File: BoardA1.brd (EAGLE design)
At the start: 43.2 x 100 mm, 17 parts, among them J1 LOAD_CELL1X03-PTH, J2 CONN_12X2, J3 LOAD_CELL1X03-PTH, J5 LOAD_CELL1X03-PTH, J6 LOAD_CELL1X03-PTH

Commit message: Starting Routing Board
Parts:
- moved C3 25.4 mm to (11.4, 59.7), turned to 180 degrees
- moved R3 23.4 mm to (31.8, 90.2), turned to 180 degrees
- moved C2 21.6 mm to (5.08, 58.4)
- moved R1 20.1 mm to (27.9, 86.4), turned to 180 degrees
- moved C4 15.2 mm to (29.2, 58.4)
- moved U$2 14.0 mm to (33.0, 71.1), turned to 270 degrees
- moved R6 7.41 mm to (8.89, 92.7), turned to 180 degrees
- moved R5 5.24 mm to (10.2, 85.1), turned to 0 degrees
- moved U$3 1.80 mm to (10.2, 71.1), turned to 270 degrees
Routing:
- net GND: track 0.00 -> 106.2 mm
- net +15V: track 0.00 -> 46.5 mm
- net -15V: track 0.00 -> 41.1 mm
- net -SIG1: track 0.00 -> 32.5 mm
- net -EX2: track 0.00 -> 29.5 mm
- net +EX2: track 0.00 -> 28.7 mm
- net -SIG2: track 0.00 -> 28.0 mm
- net -EX1: track 0.00 -> 23.6 mm
- net +EX1: track 0.00 -> 22.9 mm
- net 5V: track 0.00 -> 19.1 mm
- net +SIG2: track 0.00 -> 14.5 mm
- net +SIG1: track 0.00 -> 13.3 mm
- net N$3: track 0.00 -> 12.8 mm
- net N$1: track 0.00 -> 10.3 mm
- net N$2: track 0.00 -> 7.10 mm

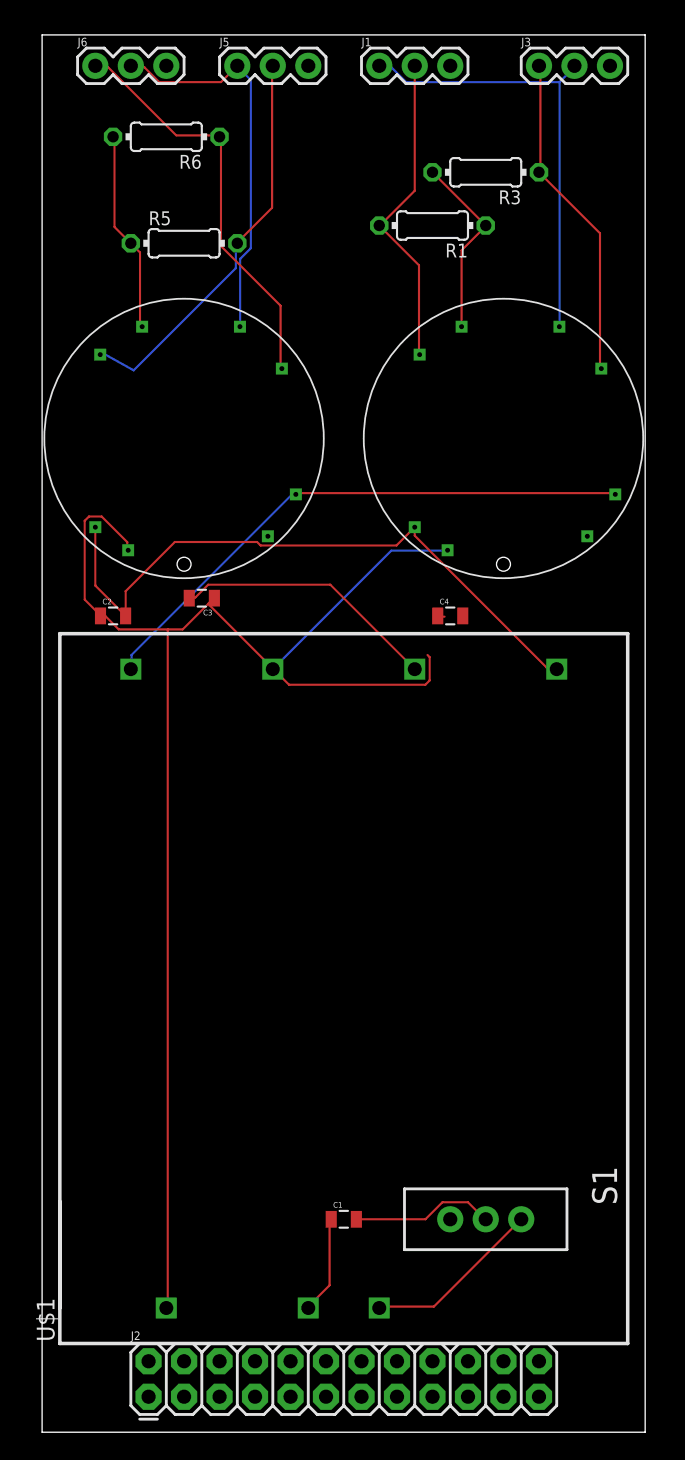
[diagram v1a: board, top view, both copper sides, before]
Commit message: routed Top Layer Board
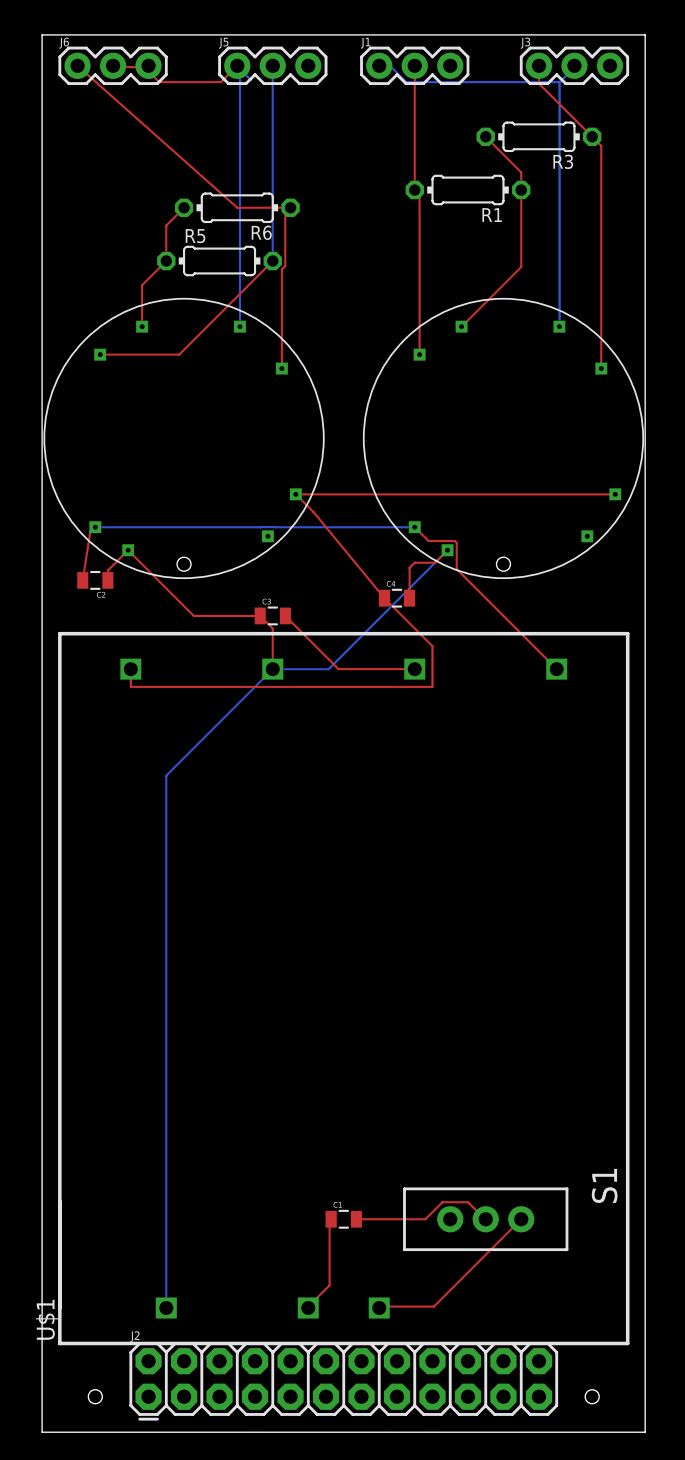
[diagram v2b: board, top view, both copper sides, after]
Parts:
- moved R6 7.18 mm to (14.0, 87.6)
- moved C3 5.24 mm to (16.5, 58.4), turned to 0 degrees
- moved R3 4.58 mm to (35.6, 92.7)
- moved C4 4.02 mm to (25.4, 59.7)
- moved R1 3.59 mm to (30.5, 88.9)
- moved R5 2.84 mm to (12.7, 83.8)
- moved C2 2.84 mm to (3.81, 61.0), turned to 180 degrees
- moved J6 1.27 mm to (2.54, 97.8)
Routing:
- net -15V: track 41.1 -> 63.3 mm
- net GND: track 106.2 -> 88.7 mm
- net 5V: track 19.1 -> 10.8 mm
- net +SIG2: track 14.5 -> 9.95 mm
- net +15V: track 46.5 -> 42.3 mm
- net +SIG1: track 13.3 -> 16.5 mm
- net -SIG2: track 28.0 -> 30.1 mm
- net +EX1: track 22.9 -> 21.0 mm
- net -EX2: track 29.5 -> 31.0 mm

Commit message: updated
added holes to attach boards
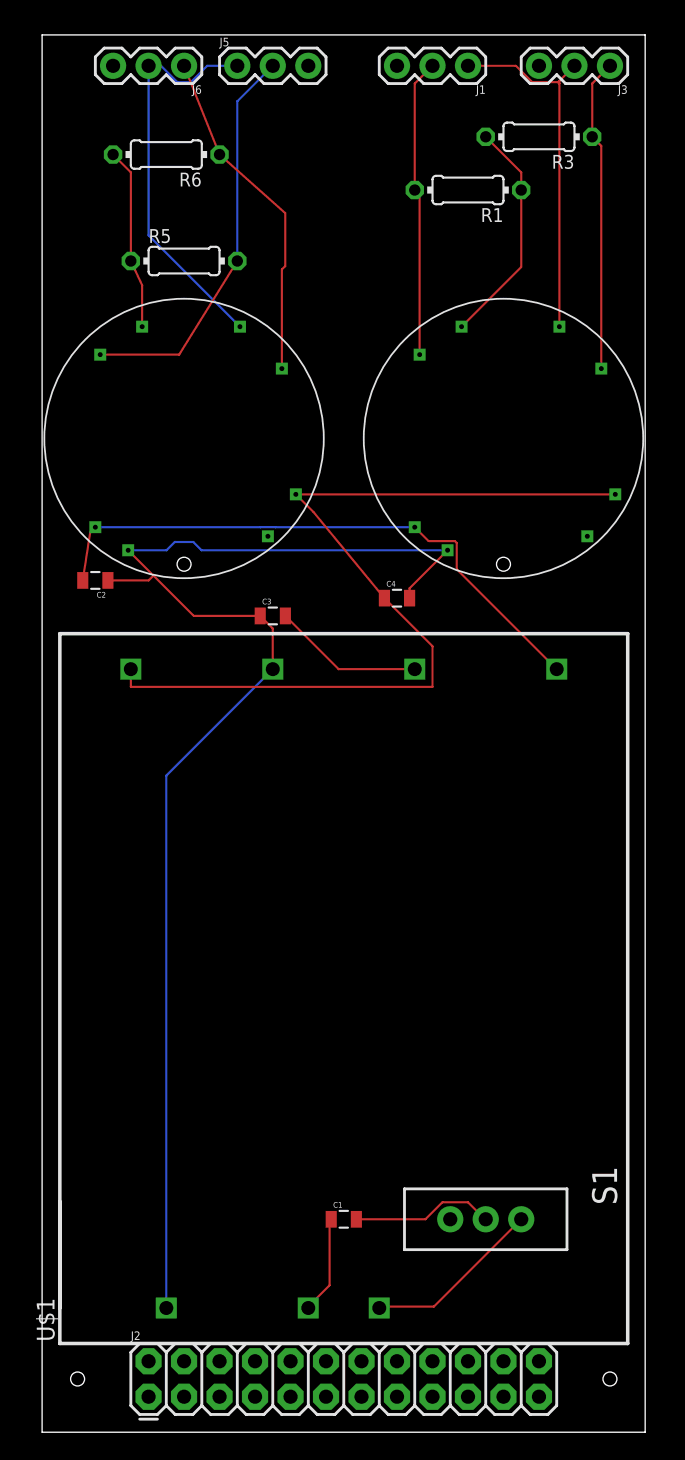
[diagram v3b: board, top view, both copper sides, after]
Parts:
- moved J6 7.62 mm to (10.2, 97.8), turned to 180 degrees
- moved J1 6.35 mm to (30.5, 97.8), turned to 180 degrees
- moved R6 6.35 mm to (8.89, 91.4)
- moved J3 5.08 mm to (40.6, 97.8), turned to 180 degrees
- moved R5 2.54 mm to (10.2, 83.8)
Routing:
- net GND: track 88.7 -> 95.8 mm
- net -EX2: track 31.0 -> 24.5 mm
- net -SIG1: track 32.5 -> 26.2 mm
- net +SIG2: track 9.95 -> 13.2 mm
- net -EX1: track 23.8 -> 22.6 mm
- net -SIG2: track 30.1 -> 29.1 mm
- net +EX2: track 29.2 -> 28.7 mm
- net +EX1: track 21.0 -> 21.5 mm

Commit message: update 2.0
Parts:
- moved J6 5.68 mm to (15.2, 95.2)
- moved R6 5.08 mm to (14.0, 91.4)
- moved J5 3.81 mm to (10.2, 97.8)
- moved R5 2.54 mm to (10.2, 86.4)
- moved J1 1.27 mm to (29.2, 97.8)
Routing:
- net -SIG2: track 29.1 -> 21.3 mm
- net -EX2: track 24.5 -> 20.4 mm
- net -SIG1: track 26.2 -> 27.5 mm
- net +SIG2: track 13.2 -> 14.2 mm
- net +EX2: track 28.7 -> 27.7 mm
- net +EX1: track 21.5 -> 21.0 mm
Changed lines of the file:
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@@
 <element name="C3" library="SparkFun-Capacitors" package="0805" value="" x="16.51" y="58.42"/>
 <element name="C4" library="SparkFun-Capacitors" package="0805" value="" x="25.4" y="59.69"/>
-<element name="J1" library="Smartcrutches" package="1X03" value="LOAD_CELL1X03-PTH" x="30.48" y="97.79" rot="R180">
-<attribute name="SF_ID" value="SEN-10245" x="30.48" y="97.79" size="1.778" layer="27" rot="R180" display="off"/>
+<element name="J1" library="Smartcrutches" package="1X03" value="LOAD_CELL1X03-PTH" x="29.21" y="97.79" rot="R180">
+<attribute name="SF_ID" value="SEN-10245" x="29.21" y="97.79" size="1.778" layer="27" rot="R180" display="off"/>
 </element>
 <element name="J3" library="Smartcrutches" package="1X03" value="LOAD_CELL1X03-PTH" x="40.64" y="97.79" rot="R180">
 <attribute name="SF_ID" value="SEN-10245" x="40.64" y="97.79" size="1.778" layer="27" rot="R180" display="off"/>
 </element>
-<element name="J5" library="Smartcrutches" package="1X03" value="LOAD_CELL1X03-PTH" x="13.97" y="97.79">
-<attribute name="SF_ID" value="SEN-10245" x="13.97" y="97.79" size="1.778" layer="27" display="off"/>
-</element>
-<element name="J6" library="Smartcrutches" package="1X03" value="LOAD_CELL1X03-PTH" x="10.16" y="97.79" rot="R180">
-<attribute name="SF_ID" value="SEN-10245" x="10.16" y="97.79" size="1.778" layer="27" rot="R180" display="off"/>
+<element name="J5" library="Smartcrutches" package="1X03" value="LOAD_CELL1X03-PTH" x="10.16" y="97.79">
+<attribute name="SF_ID" value="SEN-10245" x="10.16" y="97.79" size="1.778" layer="27" display="off"/>
+</element>
+<element name="J6" library="Smartcrutches" package="1X03" value="LOAD_CELL1X03-PTH" x="15.24" y="95.25" rot="R180">
+<attribute name="SF_ID" value="SEN-10245" x="15.24" y="95.25" size="1.778" layer="27" rot="R180" display="off"/>
 </element>
 <element name="R1" library="eagle-ltspice" library_urn="urn:adsk.eagle:library:217" package="0204/7" value="" x="30.48" y="88.9" rot="R180">
@@
 <attribute name="SPICEPREFIX" value="R" x="35.56" y="92.71" size="1.778" layer="27" rot="R180" display="off"/>
 </element>
-<element name="R5" library="eagle-ltspice" library_urn="urn:adsk.eagle:library:217" package="0204/7" value="" x="10.16" y="83.82">
-<attribute name="SPICEMODEL" value="NONE" x="10.16" y="83.82" size="1.778" layer="27" display="off"/>
-<attribute name="SPICEPREFIX" value="R" x="10.16" y="83.82" size="1.778" layer="27" display="off"/>
-</element>
-<element name="R6" library="eagle-ltspice" library_urn="urn:adsk.eagle:library:217" package="0204/7" value="" x="8.89" y="91.44" rot="R180">
-<attribute name="SPICEMODEL" value="NONE" x="8.89" y="91.44" size="1.778" layer="27" rot="R180" display="off"/>
-<attribute name="SPICEPREFIX" value="R" x="8.89" y="91.44" size="1.778" layer="27" rot="R180" display="off"/>
+<element name="R5" library="eagle-ltspice" library_urn="urn:adsk.eagle:library:217" package="0204/7" value="" x="10.16" y="86.36">
+<attribute name="SPICEMODEL" value="NONE" x="10.16" y="86.36" size="1.778" layer="27" display="off"/>
+<attribute name="SPICEPREFIX" value="R" x="10.16" y="86.36" size="1.778" layer="27" display="off"/>
+</element>
+<element name="R6" library="eagle-ltspice" library_urn="urn:adsk.eagle:library:217" package="0204/7" value="" x="13.97" y="91.44" rot="R180">
+<attribute name="SPICEMODEL" value="NONE" x="13.97" y="91.44" size="1.778" layer="27" rot="R180" display="off"/>
+<attribute name="SPICEPREFIX" value="R" x="13.97" y="91.44" size="1.778" layer="27" rot="R180" display="off"/>
 </element>
 <element name="S1" library="SparkFun-Electromechanical" package="SWITCH-SPDT" value="" x="31.75" y="15.24" rot="R270">
@@
 <wire x1="37.02" y1="96.52" x2="37.02" y2="96.71" width="0.1524" layer="1"/>
 <wire x1="37.02" y1="96.71" x2="38.1" y2="97.79" width="0.1524" layer="1"/>
-<wire x1="30.48" y1="97.79" x2="33.90763125" y2="97.79" width="0.1524" layer="1"/>
+<wire x1="29.21" y1="97.79" x2="33.90763125" y2="97.79" width="0.1524" layer="1"/>
 <wire x1="36.9184" y1="96.6216" x2="37.02" y2="96.52" width="0.1524" layer="1"/>
 <wire x1="33.90763125" y1="97.79" x2="35.07603125" y2="96.6216" width="0.1524" layer="1"/>
@@
 <wire x1="27.02" y1="77.12" x2="27.02" y2="88.55" width="0.1524" layer="1"/>
 <wire x1="27.02" y1="88.55" x2="26.67" y2="88.9" width="0.1524" layer="1"/>
-<wire x1="26.67" y1="88.9" x2="26.67" y2="96.52" width="0.1524" layer="1"/>
-<wire x1="26.67" y1="96.52" x2="27.94" y2="97.79" width="0.1524" layer="1"/>
+<wire x1="26.67" y1="88.9" x2="26.67" y2="97.79" width="0.1524" layer="1"/>
 </signal>
 <signal name="-EX2">
@@
 <wire x1="17.16" y1="76.12" x2="17.16" y2="83.2127625" width="0.1524" layer="1"/>
 <wire x1="17.16" y1="83.2127625" x2="17.399" y2="83.4517625" width="0.1524" layer="1"/>
-<wire x1="12.7" y1="91.44" x2="17.399" y2="87.249" width="0.1524" layer="1"/>
+<wire x1="17.78" y1="91.44" x2="17.399" y2="87.249" width="0.1524" layer="1"/>
 <wire x1="17.399" y1="83.4517625" x2="17.399" y2="87.249" width="0.1524" layer="1"/>
-<wire x1="10.16" y1="97.79" x2="12.7" y2="91.44" width="0.1524" layer="1"/>
+<wire x1="15.24" y1="95.25" x2="15.24" y2="93.98" width="0.1524" layer="1"/>
+<wire x1="15.24" y1="93.98" x2="17.78" y2="91.44" width="0.1524" layer="1"/>
 </signal>
 <signal name="-SIG2">
@@
 <contactref element="J6" pad="2"/>
 <contactref element="J5" pad="1"/>
-<wire x1="14.1732" y1="79.248" x2="14.16" y2="79.12" width="0.1524" layer="16"/>
-<wire x1="13.97" y1="97.79" x2="14.16" y2="97.6" width="0.1524" layer="16"/>
-<wire x1="9.67603125" y1="96.6216" x2="10.64396875" y2="96.6216" width="0.1524" layer="16"/>
-<wire x1="7.62" y1="97.79" x2="8.50763125" y2="97.79" width="0.1524" layer="16"/>
-<wire x1="11.81236875" y1="97.79" x2="13.97" y2="97.79" width="0.1524" layer="16"/>
-<wire x1="8.50763125" y1="97.79" x2="9.67603125" y2="96.6216" width="0.1524" layer="16"/>
-<wire x1="10.64396875" y1="96.6216" x2="11.81236875" y2="97.79" width="0.1524" layer="16"/>
-<wire x1="14.16" y1="79.12" x2="7.62" y2="85.66" width="0.1524" layer="16"/>
-<wire x1="7.62" y1="85.66" x2="7.62" y2="97.79" width="0.1524" layer="16"/>
+<wire x1="14.16" y1="79.12" x2="14.1732" y2="79.248" width="0.1524" layer="16"/>
+<wire x1="9.77763125" y1="96.52" x2="9.67603125" y2="96.6216" width="0.1524" layer="16"/>
+<wire x1="12.7" y1="92.6972375" x2="12.7" y2="95.25" width="0.1524" layer="16"/>
+<wire x1="12.7" y1="92.6972375" x2="11.811" y2="91.8082375" width="0.1524" layer="16"/>
+<wire x1="11.811" y1="91.8082375" x2="11.811" y2="81.469" width="0.1524" layer="16"/>
+<wire x1="11.811" y1="81.469" x2="14.16" y2="79.12" width="0.1524" layer="16"/>
+<wire x1="12.7" y1="95.25" x2="10.16" y2="97.79" width="0.1524" layer="16"/>
+<wire x1="10.16" y1="97.79" x2="9.67603125" y2="96.6216" width="0" layer="19" extent="16-16"/>
 </signal>
 <signal name="+SIG2">
@@
 <wire x1="7.0104" y1="79.248" x2="7.16" y2="79.12" width="0.1524" layer="1"/>
 <wire x1="7.16" y1="79.12" x2="7.16" y2="82.09" width="0.1524" layer="1"/>
-<wire x1="7.16" y1="82.09" x2="6.35" y2="83.82" width="0.1524" layer="1"/>
-<wire x1="6.35" y1="83.82" x2="6.35" y2="90.17" width="0.1524" layer="1"/>
-<wire x1="6.35" y1="90.17" x2="5.08" y2="91.44" width="0.1524" layer="1"/>
+<wire x1="7.16" y1="82.09" x2="6.35" y2="86.36" width="0.1524" layer="1"/>
+<wire x1="6.35" y1="86.36" x2="6.35" y2="87.63" width="0.1524" layer="1"/>
+<wire x1="6.35" y1="87.63" x2="10.16" y2="91.44" width="0.1524" layer="1"/>
 </signal>
 <signal name="+EX2">
@@
 <contactref element="R5" pad="2"/>
 <contactref element="J5" pad="2"/>
-<wire x1="16.51" y1="97.79" x2="16.4592" y2="97.6884" width="0.1524" layer="1"/>
 <wire x1="4.16" y1="77.12" x2="9.81" y2="77.12" width="0.1524" layer="1"/>
-<wire x1="9.81" y1="77.12" x2="13.97" y2="83.82" width="0.1524" layer="1"/>
-<wire x1="13.97" y1="83.82" x2="13.97" y2="95.25" width="0.1524" layer="16"/>
-<wire x1="13.97" y1="95.25" x2="16.51" y2="97.79" width="0.1524" layer="16"/>
+<wire x1="9.81" y1="77.12" x2="13.97" y2="86.36" width="0.1524" layer="1"/>
+<wire x1="13.97" y1="86.36" x2="13.97" y2="96.52" width="0.1524" layer="16"/>
+<wire x1="13.97" y1="96.52" x2="12.7" y2="97.79" width="0.1524" layer="16"/>
 </signal>
 <signal name="N$4">

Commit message: Updated both Boards
- Added holes
- Changed connectors
- routed both Boards
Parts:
- J2: value CONN_12X2 -> FEMALE 2x3; device Smartcrutches:2X12 -> SparkFun-Connectors:2X3
- moved J2 14.4 mm to (22.0, 2.00)
- moved J3 2.54 mm to (38.1, 97.8)
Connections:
- net 5V: now also J2.1
- net GND: now also J2.3
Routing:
- net 5V: track 10.8 -> 65.5 mm
- net GND: track 95.8 -> 114.3 mm
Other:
- board size 43.2 x 100 mm -> 44 x 100.5 mm
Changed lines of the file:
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@@
 <board>
 <plain>
-<wire x1="0" y1="0" x2="43.16" y2="0" width="0" layer="20"/>
-<wire x1="43.16" y1="0" x2="43.16" y2="100" width="0" layer="20"/>
-<wire x1="43.16" y1="100" x2="0" y2="100" width="0" layer="20"/>
+<wire x1="0" y1="0" x2="44" y2="0" width="0" layer="20"/>
+<wire x1="44" y1="0" x2="44" y2="100.5" width="0" layer="20"/>
+<wire x1="44" y1="100.5" x2="0" y2="100" width="0" layer="20"/>
 <wire x1="0" y1="100" x2="0" y2="0" width="0" layer="20"/>
-<hole x="2.54" y="3.81" drill="1"/>
+<hole x="2" y="3" drill="1"/>
 <hole x="40.64" y="3.81" drill="1"/>
+<hole x="42" y="97.5" drill="1"/>
+<hole x="2" y="97.5" drill="1"/>
 </plain>
 <attributes>
@@
 <attribute name="SF_ID" value="SEN-10245" x="29.21" y="97.79" size="1.778" layer="27" rot="R180" display="off"/>
 </element>
-<element name="J3" library="Smartcrutches" package="1X03" value="LOAD_CELL1X03-PTH" x="40.64" y="97.79" rot="R180">
-<attribute name="SF_ID" value="SEN-10245" x="40.64" y="97.79" size="1.778" layer="27" rot="R180" display="off"/>
+<element name="J3" library="Smartcrutches" package="1X03" value="LOAD_CELL1X03-PTH" x="38.1" y="97.79" rot="R180">
+<attribute name="SF_ID" value="SEN-10245" x="38.1" y="97.79" size="1.778" layer="27" rot="R180" display="off"/>
 </element>
 <element name="J5" library="Smartcrutches" package="1X03" value="LOAD_CELL1X03-PTH" x="10.16" y="97.79">
@@
 <element name="U$2" library="Smartcrutches" package="ICA3H" value="ICA3H" x="33.02" y="71.12" rot="R270"/>
 <element name="U$3" library="Smartcrutches" package="ICA3H" value="ICA3H" x="10.16" y="71.12" rot="R270"/>
-<element name="J2" library="Smartcrutches" package="2X12" value="CONN_12X2" x="7.62" y="2.54"/>
+<element name="J2" library="SparkFun-Connectors" package="2X3" value="FEMALE 2x3" x="22" y="2">
+<attribute name="PROD_ID" value="CONN-11566" x="22" y="2" size="1.778" layer="27" display="off"/>
+</element>
 </elements>
 <signals>
@@
 <wire x1="26.3" y1="59.69" x2="26.3" y2="60.4" width="0.1524" layer="1"/>
 <wire x1="26.3" y1="60.4" x2="29.02" y2="63.12" width="0.1524" layer="1"/>
+<contactref element="J2" pad="3"/>
+<wire x1="23.1684" y1="3.3716" x2="24.54" y2="2" width="0.1524" layer="1"/>
+<wire x1="21.51603125" y1="3.3716" x2="23.1684" y2="3.3716" width="0.1524" layer="1"/>
+<wire x1="8.89" y1="8.89" x2="15.99763125" y2="8.89" width="0.1524" layer="1"/>
+<wire x1="15.99763125" y1="8.89" x2="21.51603125" y2="3.3716" width="0.1524" layer="1"/>
 </signal>
 <signal name="+15V">
@@
 <wire x1="26.67" y1="54.61" x2="21.22" y2="54.61" width="0.1524" layer="1"/>
 <wire x1="21.22" y1="54.61" x2="17.41" y2="58.42" width="0.1524" layer="1"/>
+<contactref element="J2" pad="1"/>
+<wire x1="23.1684" y1="4.05603125" x2="23.1684" y2="5.02396875" width="0.1524" layer="16"/>
+<wire x1="23.1684" y1="5.02396875" x2="22.986184375" y2="5.206184375" width="0.1524" layer="16"/>
+<wire x1="22" y1="2" x2="22" y2="2.88763125" width="0.1524" layer="16"/>
+<wire x1="22" y1="2.88763125" x2="23.1684" y2="4.05603125" width="0.1524" layer="16"/>
+<wire x1="22.986184375" y1="5.206184375" x2="22.986184375" y2="50.926184375" width="0.1524" layer="16"/>
+<wire x1="22.986184375" y1="50.926184375" x2="26.67" y2="54.61" width="0.1524" layer="16"/>
 </signal>
 <signal name="-15V">
@@
 <wire x1="40.02" y1="92.06" x2="39.37" y2="92.71" width="0.1524" layer="1"/>
 <wire x1="39.37" y1="92.71" x2="39.37" y2="96.52" width="0.1524" layer="1"/>
-<wire x1="39.37" y1="96.52" x2="40.64" y2="97.79" width="0.1524" layer="1"/>
+<wire x1="39.37" y1="96.52" x2="38.1" y2="97.79" width="0.1524" layer="1"/>
 </signal>
 <signal name="-SIG1">
@@
 <wire x1="37.02" y1="96.52" x2="37.02" y2="79.12" width="0.1524" layer="1"/>
 <wire x1="37.02" y1="96.52" x2="37.02" y2="96.71" width="0.1524" layer="1"/>
-<wire x1="37.02" y1="96.71" x2="38.1" y2="97.79" width="0.1524" layer="1"/>
+<wire x1="37.02" y1="96.71" x2="35.56" y2="97.79" width="0.1524" layer="1"/>
 <wire x1="29.21" y1="97.79" x2="33.90763125" y2="97.79" width="0.1524" layer="1"/>
 <wire x1="36.9184" y1="96.6216" x2="37.02" y2="96.52" width="0.1524" layer="1"/>
